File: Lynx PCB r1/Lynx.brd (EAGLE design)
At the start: 124.3 x 53.1 mm, 110 parts, among them IC1 LM321MF, IC3 ICL7660, Q1 8MHz

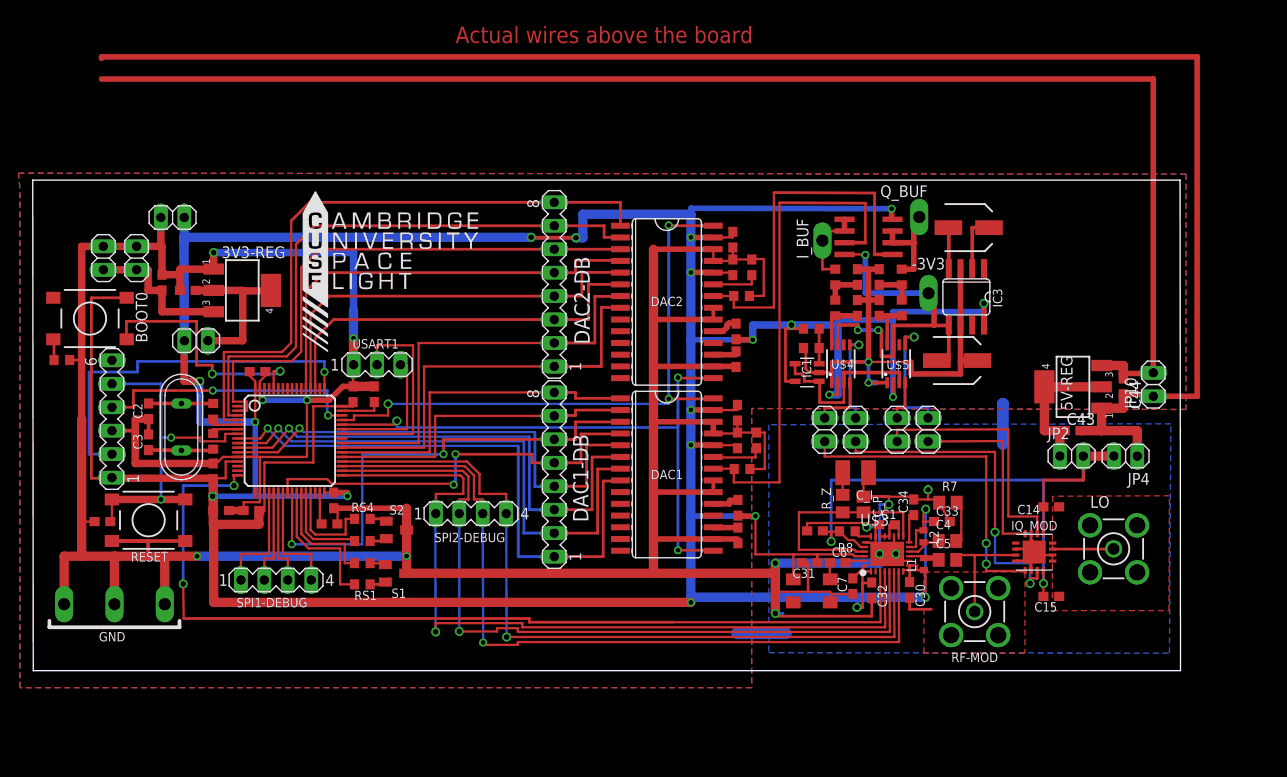
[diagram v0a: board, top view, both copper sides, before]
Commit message: more silk
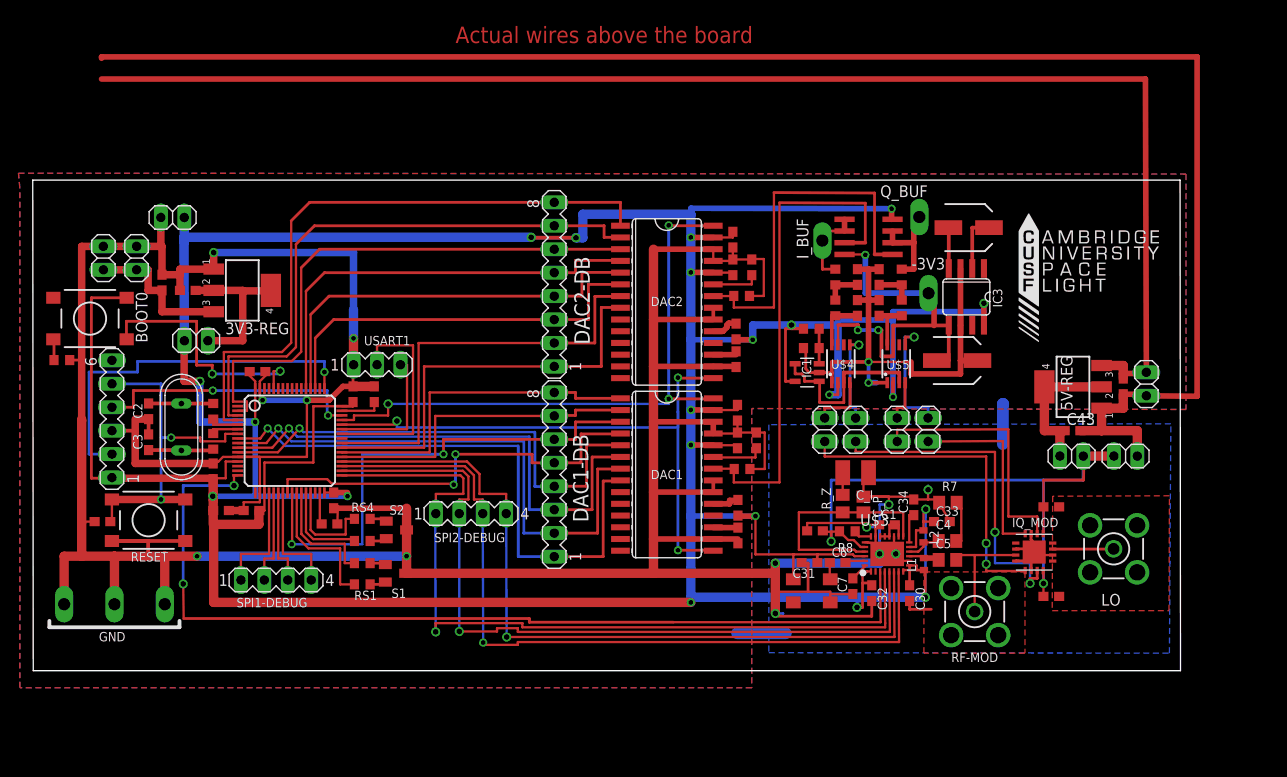
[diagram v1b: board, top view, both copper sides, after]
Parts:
- U$2: device Lynx components:CUSF_LOGO_LARGE -> Lynx components:CUSF_LOGO
- moved U$2 77.6 mm to (106.6, 35.5)
- moved JP10 0.75 mm to (120.6, 31.1)
- moved C30 0.35 mm to (95.0, 8.40)
- moved C32 0.30 mm to (90.8, 8.40)
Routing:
- net GND: track 747.8 -> 748.5 mm
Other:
- board text added: "Dev Board: r1"
- board text added: "Joe Roberts - Jul2013"
- board text removed: "Developement Board"
- board text removed: "Joe Roberts"
- board text removed: "r1"

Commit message: Finished first pass of silk
Finished organizing the first revision of the artwork. Added pin names
to all busses. Created a dac-clk test pin
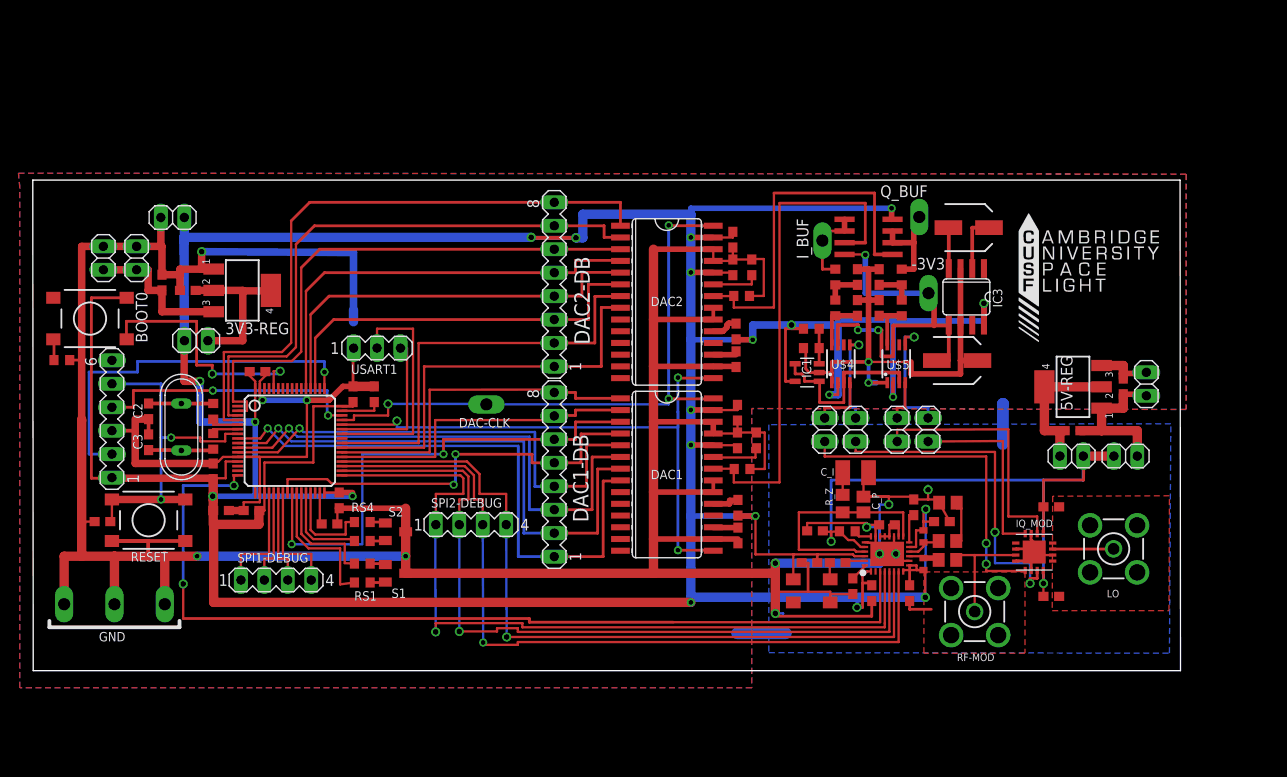
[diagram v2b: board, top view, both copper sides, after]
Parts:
- added DAC-CLK: PTR1PAD1-13Y, testpad:P1-13Y
- moved USART1 1.80 mm to (37.2, 35.0)
- moved SPI2-DEBUG 1.20 mm to (47.4, 15.8)
- moved C19 0.60 mm to (33.1, 18.4)
- moved RS3 0.35 mm to (35.6, 16.1)
- moved S2 0.22 mm to (39.2, 15.1)
- moved RS2 0.20 mm to (35.6, 9.55)
- moved RS1 0.05 mm to (35.6, 11.6)
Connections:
- net DAC-CLK: now also DAC-CLK.TP
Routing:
- net GND: track 748.5 -> 586.5 mm, vias 15 -> 14
- net POWER-IN: track 169.2 -> 24.3 mm
- net SPI2-CS: track 89.1 -> 91.4 mm
- net USART1_RX: track 14.7 -> 16.6 mm
- net USART1_TX: track 23.3 -> 25.1 mm
- net +3V3: track 514.0 -> 515.1 mm
- net DAC-CLK: track 66.2 -> 66.9 mm
- net DAC1-DB7: track 37.3 -> 37.9 mm
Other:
- board text added: "CLK"
- board text added: "CS"
- board text added: "DB0"
- board text added: "DB7"
- board text added: "GND"
- board text added: "MISO"
- board text added: "MOSI"
- board text added: "STM-RX"
- board text added: "STM-TX"
- board text added: "TXCO"
- board text removed: "Actual wires above the board"

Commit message: Gerbers
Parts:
- moved C17 0.30 mm to (35.0, 29.9)
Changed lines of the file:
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@@
 <layer number="20" name="Dimension" color="15" fill="1" visible="yes" active="yes"/>
 <layer number="21" name="tPlace" color="7" fill="1" visible="yes" active="yes"/>
-<layer number="22" name="bPlace" color="7" fill="1" visible="no" active="yes"/>
+<layer number="22" name="bPlace" color="7" fill="1" visible="yes" active="yes"/>
 <layer number="23" name="tOrigins" color="15" fill="1" visible="yes" active="yes"/>
-<layer number="24" name="bOrigins" color="15" fill="1" visible="no" active="yes"/>
+<layer number="24" name="bOrigins" color="15" fill="1" visible="yes" active="yes"/>
 <layer number="25" name="tNames" color="7" fill="1" visible="yes" active="yes"/>
-<layer number="26" name="bNames" color="7" fill="1" visible="no" active="yes"/>
+<layer number="26" name="bNames" color="7" fill="1" visible="yes" active="yes"/>
 <layer number="27" name="tValues" color="7" fill="1" visible="yes" active="yes"/>
-<layer number="28" name="bValues" color="7" fill="1" visible="no" active="yes"/>
-<layer number="29" name="tStop" color="7" fill="3" visible="no" active="yes"/>
+<layer number="28" name="bValues" color="7" fill="1" visible="yes" active="yes"/>
+<layer number="29" name="tStop" color="7" fill="3" visible="yes" active="yes"/>
 <layer number="30" name="bStop" color="7" fill="6" visible="no" active="yes"/>
-<layer number="31" name="tCream" color="7" fill="4" visible="no" active="yes"/>
+<layer number="31" name="tCream" color="7" fill="4" visible="yes" active="yes"/>
 <layer number="32" name="bCream" color="7" fill="5" visible="no" active="yes"/>
 <layer number="33" name="tFinish" color="6" fill="3" visible="no" active="yes"/>
@@
 <layer number="37" name="tTest" color="7" fill="1" visible="no" active="yes"/>
 <layer number="38" name="bTest" color="7" fill="1" visible="no" active="yes"/>
-<layer number="39" name="tKeepout" color="4" fill="11" visible="no" active="yes"/>
-<layer number="40" name="bKeepout" color="1" fill="11" visible="no" active="yes"/>
-<layer number="41" name="tRestrict" color="4" fill="10" visible="no" active="yes"/>
-<layer number="42" name="bRestrict" color="1" fill="10" visible="no" active="yes"/>
-<layer number="43" name="vRestrict" color="2" fill="10" visible="no" active="yes"/>
-<layer number="44" name="Drills" color="7" fill="1" visible="no" active="yes"/>
-<layer number="45" name="Holes" color="7" fill="1" visible="no" active="yes"/>
-<layer number="46" name="Milling" color="3" fill="1" visible="no" active="yes"/>
-<layer number="47" name="Measures" color="7" fill="1" visible="no" active="yes"/>
+<layer number="39" name="tKeepout" color="4" fill="11" visible="yes" active="yes"/>
+<layer number="40" name="bKeepout" color="1" fill="11" visible="yes" active="yes"/>
+<layer number="41" name="tRestrict" color="4" fill="10" visible="yes" active="yes"/>
+<layer number="42" name="bRestrict" color="1" fill="10" visible="yes" active="yes"/>
+<layer number="43" name="vRestrict" color="2" fill="10" visible="yes" active="yes"/>
+<layer number="44" name="Drills" color="7" fill="1" visible="yes" active="yes"/>
+<layer number="45" name="Holes" color="7" fill="1" visible="yes" active="yes"/>
+<layer number="46" name="Milling" color="3" fill="1" visible="yes" active="yes"/>
+<layer number="47" name="Measures" color="7" fill="1" visible="yes" active="yes"/>
 <layer number="48" name="Document" color="7" fill="1" visible="yes" active="yes"/>
 <layer number="49" name="Reference" color="7" fill="1" visible="yes" active="yes"/>
 <layer number="50" name="dxf" color="7" fill="1" visible="no" active="no"/>
 <layer number="51" name="tDocu" color="7" fill="1" visible="yes" active="yes"/>
-<layer number="52" name="bDocu" color="7" fill="1" visible="no" active="yes"/>
+<layer number="52" name="bDocu" color="7" fill="1" visible="yes" active="yes"/>
 <layer number="53" name="tGND_GNDA" color="7" fill="9" visible="no" active="no"/>
 <layer number="54" name="bGND_GNDA" color="1" fill="9" visible="no" active="no"/>
@@
 <attribute name="VALUE" x="26.685" y="34.255" size="1.016" layer="27" font="vector" ratio="12" rot="R180"/>
 </element>
-<element name="C17" library="rcl" package="C0603" value="0.1uF" x="34.65" y="29.95" smashed="yes" rot="R270">
-<attribute name="ARM" x="34.65" y="29.95" size="1.778" layer="27" rot="R270" display="off"/>
-<attribute name="VALUE" x="33.805" y="29.165" size="0.8128" layer="27" font="vector" ratio="12" rot="R90"/>
+<element name="C17" library="rcl" package="C0603" value="0.1uF" x="34.95" y="29.95" smashed="yes" rot="R270">
+<attribute name="ARM" x="34.95" y="29.95" size="1.778" layer="27" rot="R270" display="off"/>
+<attribute name="VALUE" x="34.105" y="29.165" size="0.8128" layer="27" font="vector" ratio="12" rot="R90"/>
 </element>
 <element name="C18" library="rcl" package="C0603" value="0.1uF" x="23.65" y="17.35" smashed="yes">
@@
 <attribute name="VALUE" x="31.239" y="16.382" size="1.016" layer="27" font="vector" ratio="12" rot="R180"/>
 </element>
-<element name="C22" library="resistor" package="C0603" value="2.2uF" x="36.95" y="29.95" smashed="yes" rot="R90">
-<attribute name="VALUE" x="37.761" y="30.418" size="0.8128" layer="27" font="vector" ratio="12"/>
+<element name="C22" library="resistor" package="C0603" value="2.2uF" x="37" y="29.95" smashed="yes" rot="R90">
+<attribute name="VALUE" x="37.811" y="30.418" size="0.8128" layer="27" font="vector" ratio="12"/>
 </element>
 <element name="C23" library="rcl" package="C0603" value="4.7uF" x="20.35" y="17.35" smashed="yes" rot="R180">
@@
 <wire x1="24.85" y1="29.3" x2="24.55" y2="29.25" width="0.3048" layer="1"/>
 <wire x1="24.55" y1="29.25" x2="24.55" y2="30.56" width="0.254" layer="1"/>
+<wire x1="34.95" y1="30.8" x2="34.65" y2="30.8" width="0.3048" layer="1"/>
 <wire x1="34.65" y1="30.8" x2="34.65" y2="34.95" width="0.3048" layer="1"/>
 <wire x1="34.65" y1="34.95" x2="34.71" y2="34.95" width="0.3048" layer="1"/>
-<wire x1="34.65" y1="30.8" x2="33.55" y2="30.8" width="0.6096" layer="1"/>
+<wire x1="34.95" y1="30.8" x2="33.55" y2="30.8" width="0.6096" layer="1"/>
 <wire x1="33.55" y1="30.8" x2="32.05" y2="29.3" width="0.6096" layer="1"/>
 <wire x1="32.05" y1="29.3" x2="29.65" y2="29.3" width="0.6096" layer="1"/>
@@
 <contactref element="JP4" pad="1"/>
 <contactref element="JP5" pad="1"/>
-<wire x1="34.65" y1="30.8" x2="36.95" y2="30.8" width="1.016" layer="1"/>
+<wire x1="34.95" y1="30.8" x2="37" y2="30.8" width="1.016" layer="1"/>
 <contactref element="5V-REG" pad="1"/>
 <contactref element="3V3-REG" pad="1"/>
@@
 <contactref element="LO" pad="5"/>
 <polygon width="0.4064" layer="1" isolate="0.254">
-<vertex x="110.45" y="18.9"/>
-<vertex x="110.4" y="6.5"/>
-<vertex x="123.05" y="6.5"/>
-<vertex x="123.1" y="18.95"/>
+<vertex x="80.2" y="21.15"/>
+<vertex x="80.15" y="0.1"/>
+<vertex x="124.75" y="0.05"/>
+<vertex x="124.8" y="20.95"/>
+<vertex x="107.95" y="20.95"/>
+<vertex x="107.95" y="26.65"/>
+<vertex x="80.05" y="26.65"/>
 </polygon>
 <wire x1="92.52" y1="12.65" x2="93.26" y2="12.65" width="0.254" layer="1"/>
@@
 <wire x1="83.25" y1="11.65" x2="83.95" y2="11.65" width="0.3048" layer="1"/>
 <wire x1="83.95" y1="11.65" x2="83.95" y2="8.55" width="0.3048" layer="1"/>
-<polygon width="0.3048" layer="1">
-<vertex x="96.55" y="10.7"/>
-<vertex x="107.45" y="10.7"/>
-<vertex x="107.45" y="1.9"/>
-<vertex x="96.5" y="1.9"/>
-<vertex x="96.5" y="10.35"/>
-</polygon>
 <wire x1="94.95" y1="7.55" x2="94.95" y2="6.65" width="0.3048" layer="1"/>
 <wire x1="94.95" y1="6.65" x2="97.3" y2="6.65" width="0.3048" layer="1"/>
@@
 <wire x1="13.83" y1="45.97" x2="13.95" y2="45.97" width="0.8128" layer="1"/>
 <wire x1="13.95" y1="45.97" x2="13.95" y2="42.9" width="0.8128" layer="1"/>
-<polygon width="0.3048" layer="1" isolate="0.3048">
+<polygon width="0.3048" layer="1" isolate="0.6096">
 <vertex x="-1.6" y="53.9"/>
 <vertex x="124.9" y="53.8"/>
-<vertex x="124.9" y="28.3"/>
+<vertex x="124.9" y="21.9"/>
+<vertex x="122.6" y="21.9"/>
+<vertex x="122.6" y="21.85"/>
+<vertex x="108.7" y="21.85"/>
+<vertex x="108.7" y="28.8"/>
 <vertex x="77.85" y="28.4"/>
 <vertex x="77.85" y="-1.85"/>
@@
 <vertex x="-1.45" y="52.3"/>
 </polygon>
-<polygon width="0.3048" layer="16" isolate="0.3048">
+<polygon width="0.3048" layer="16" isolate="0.6096">
 <vertex x="-1.6" y="53.9"/>
 <vertex x="124.9" y="53.8"/>
@@
 <via x="24.05" y="26.95" extent="1-16" drill="0.5"/>
 <wire x1="24.05" y1="26.95" x2="24.05" y2="18.9" width="0.6096" layer="16"/>
-<wire x1="34.65" y1="29.1" x2="34.65" y2="28.66" width="0.254" layer="1"/>
+<wire x1="34.95" y1="29.1" x2="34.65" y2="28.66" width="0.254" layer="1"/>
 <wire x1="34.65" y1="28.65" x2="30.35" y2="28.65" width="0.254" layer="1"/>
 <wire x1="30.35" y1="28.65" x2="30.35" y2="22.55" width="0.254" layer="1"/>
@@
 <contactref element="U$1" pad="47"/>
 <contactref element="C22" pad="1"/>
-<wire x1="33.45" y1="28.16" x2="36.95" y2="28.16" width="0.254" layer="1"/>
-<wire x1="36.95" y1="28.16" x2="36.95" y2="29.1" width="0.254" layer="1"/>
+<wire x1="33.45" y1="28.16" x2="37" y2="28.16" width="0.254" layer="1"/>
+<wire x1="37" y1="28.16" x2="37" y2="29.1" width="0.254" layer="1"/>
 </signal>
 <signal name="N$33">
@@
 <wire x1="69.85" y1="26.35" x2="39.4" y2="26.35" width="0.254" layer="16"/>
 <wire x1="39.4" y1="26.35" x2="39.4" y2="27.05" width="0.254" layer="16"/>
-<via x="39.4" y="27.05" extent="1-16" drill="0.6"/>
+<via x="39.4" y="27.05" extent="1-16" drill="0.6" alwaysstop="yes"/>
 <wire x1="39.4" y1="27.05" x2="39.4" y2="26.66" width="0.254" layer="1"/>
 <wire x1="39.4" y1="26.66" x2="33.45" y2="26.66" width="0.254" layer="1"/>
